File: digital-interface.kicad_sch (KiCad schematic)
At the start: 33 parts, among them U701 Si8641BD-B-IS2, U702 R05C05TE05S

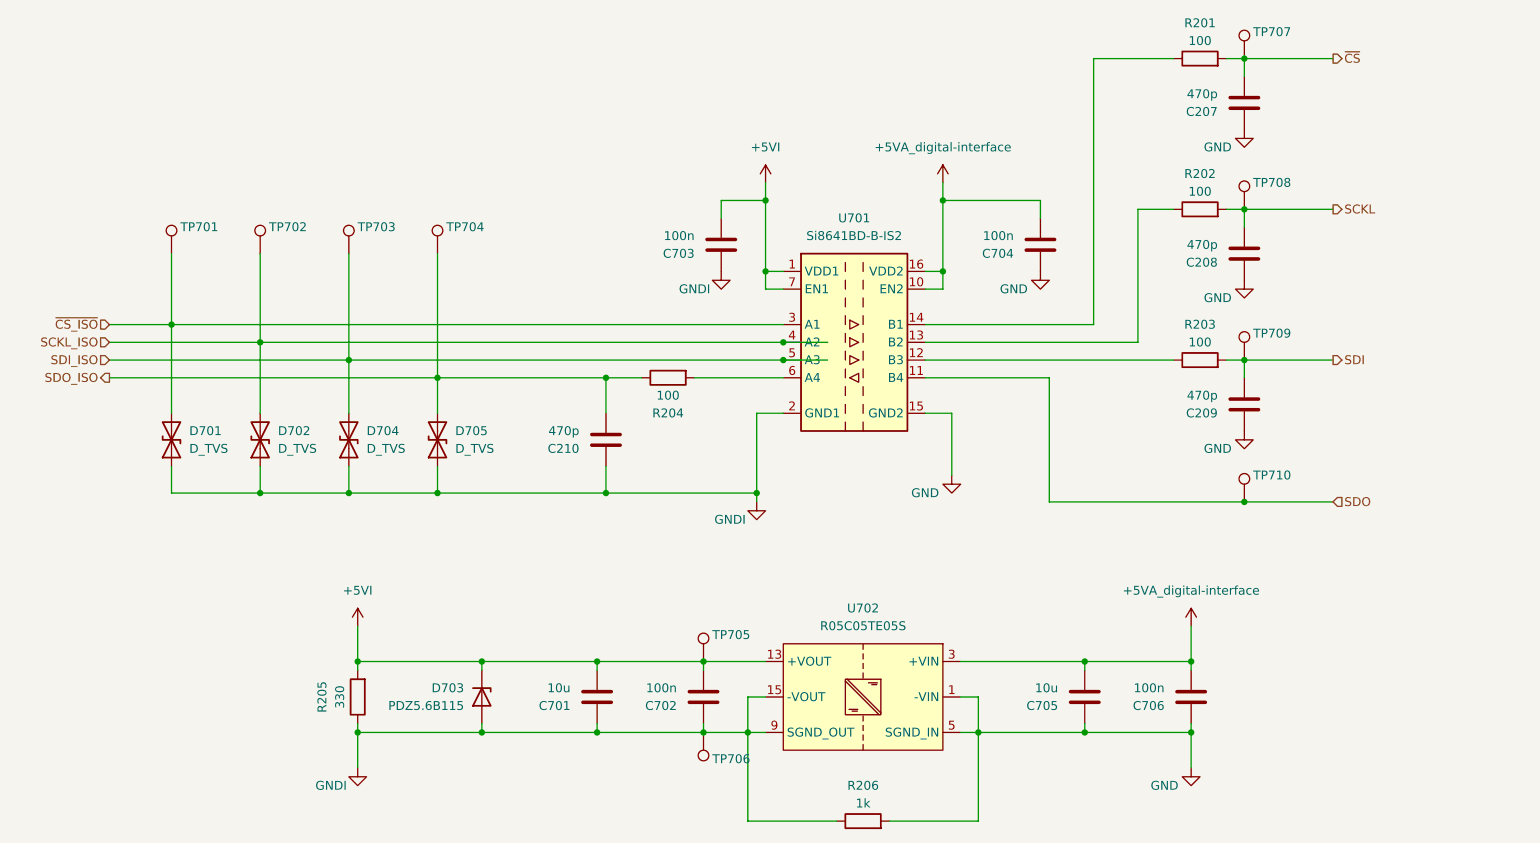
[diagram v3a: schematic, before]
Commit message: reannotate enclosure digital-interface
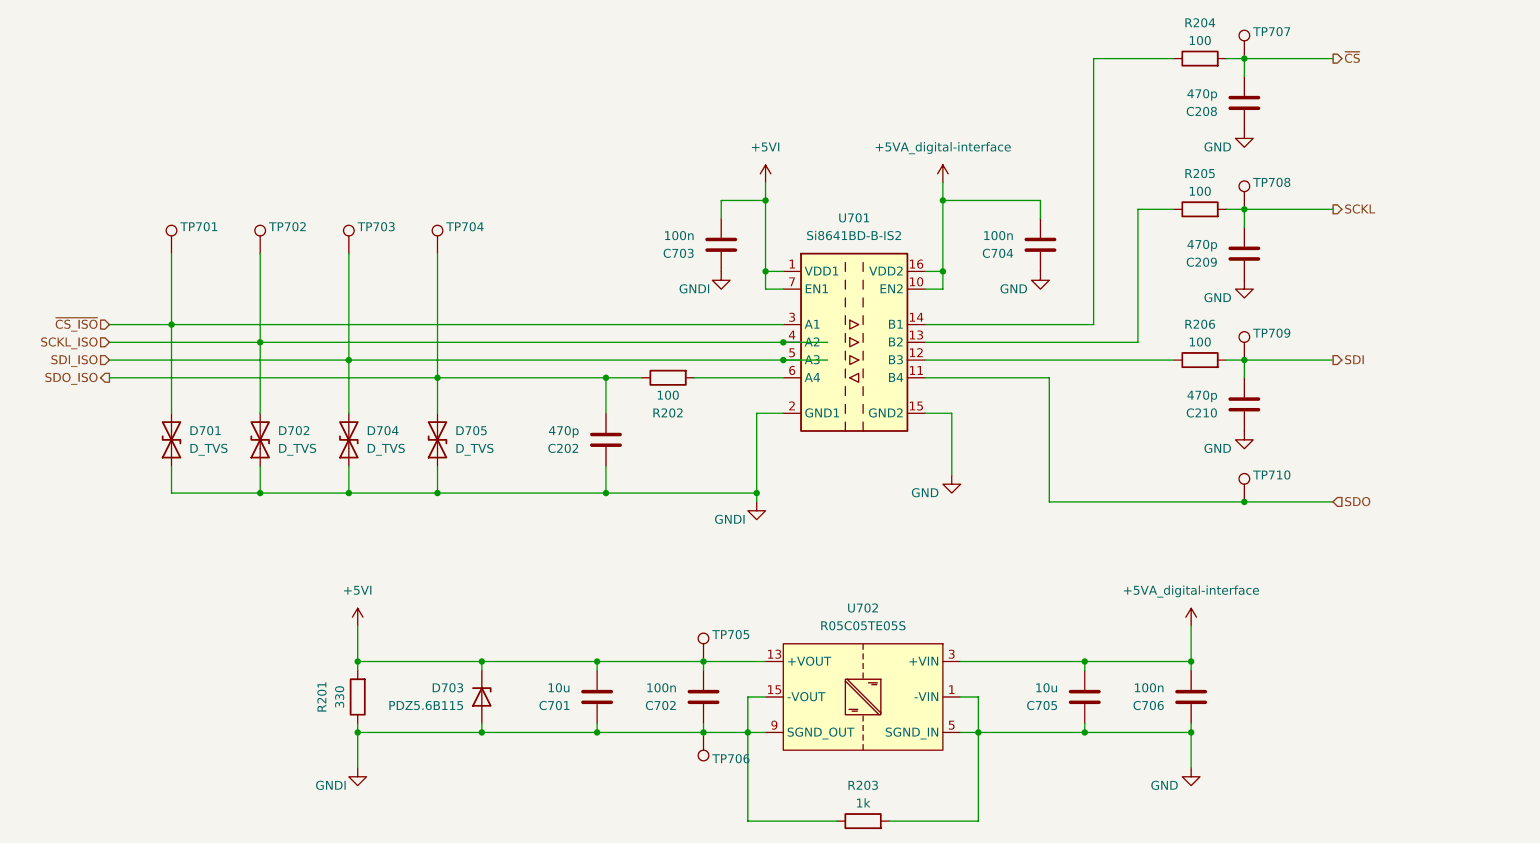
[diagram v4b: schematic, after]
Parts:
- renumbered C210 to C202, C207 to C208, C208 to C209, C209 to C210, R205 to R201, R204 to R202, R206 to R203, R201 to R204, R202 to R205, R203 to R206
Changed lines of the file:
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@@
 		(on_board yes)
 		(dnp no)
-		(property "Reference" "C207"
+		(property "Reference" "C208"
 			(at 199.39 38.1001 0)
 			(effects
@@
 			(project "enclosure"
 				(path "/8ec0899b-9d7b-491d-933a-49b74b34a0df/dc44c087-3b63-4db9-8fc8-89acb3b8154a"
-					(reference "C207")
+					(reference "C208")
 					(unit 1)
 				)
@@
 			(project "enclosure"
 				(path "/8ec0899b-9d7b-491d-933a-49b74b34a0df/dc44c087-3b63-4db9-8fc8-89acb3b8154a"
-					(reference "C206")
+					(reference "C207")
 					(unit 1)
 				)
@@
 			(project "enclosure"
 				(path "/8ec0899b-9d7b-491d-933a-49b74b34a0df/dc44c087-3b63-4db9-8fc8-89acb3b8154a"
-					(reference "#PWR204")
+					(reference "#PWR0204")
 					(unit 1)
 				)
@@
 			(project "enclosure"
 				(path "/8ec0899b-9d7b-491d-933a-49b74b34a0df/dc44c087-3b63-4db9-8fc8-89acb3b8154a"
-					(reference "C204")
+					(reference "C205")
 					(unit 1)
 				)
@@
 			(project "enclosure"
 				(path "/8ec0899b-9d7b-491d-933a-49b74b34a0df/dc44c087-3b63-4db9-8fc8-89acb3b8154a"
-					(reference "#PWR209")
+					(reference "#PWR0209")
 					(unit 1)
 				)
@@
 			(project "enclosure"
 				(path "/8ec0899b-9d7b-491d-933a-49b74b34a0df/dc44c087-3b63-4db9-8fc8-89acb3b8154a"
-					(reference "#PWR206")
+					(reference "#PWR0206")
 					(unit 1)
 				)
@@
 		(on_board yes)
 		(dnp no)
-		(property "Reference" "R204"
+		(property "Reference" "R202"
 			(at 120.65 81.28 90)
 			(effects
@@
 			(project "enclosure"
 				(path "/8ec0899b-9d7b-491d-933a-49b74b34a0df/dc44c087-3b63-4db9-8fc8-89acb3b8154a"
-					(reference "R204")
+					(reference "R202")
 					(unit 1)
 				)
@@
 			(project "enclosure"
 				(path "/8ec0899b-9d7b-491d-933a-49b74b34a0df/dc44c087-3b63-4db9-8fc8-89acb3b8154a"
-					(reference "C205")
+					(reference "C206")
 					(unit 1)
 				)
@@
 		(on_board yes)
 		(dnp no)
-		(property "Reference" "R206"
+		(property "Reference" "R203"
 			(at 148.59 134.62 90)
 			(effects
@@
 			(project "enclosure"
 				(path "/8ec0899b-9d7b-491d-933a-49b74b34a0df/dc44c087-3b63-4db9-8fc8-89acb3b8154a"
-					(reference "R206")
+					(reference "R203")
 					(unit 1)
 				)
@@
 			(project "enclosure"
 				(path "/8ec0899b-9d7b-491d-933a-49b74b34a0df/dc44c087-3b63-4db9-8fc8-89acb3b8154a"
-					(reference "#PWR210")
+					(reference "#PWR0210")
 					(unit 1)
 				)
@@
 		(on_board yes)
 		(dnp no)
-		(property "Reference" "R201"
+		(property "Reference" "R204"
 			(at 196.85 25.4 90)
 			(effects
@@
 			(project "enclosure"
 				(path "/8ec0899b-9d7b-491d-933a-49b74b34a0df/dc44c087-3b63-4db9-8fc8-89acb3b8154a"
-					(reference "R201")
+					(reference "R204")
 					(unit 1)
 				)
@@
 			(project "enclosure"
 				(path "/8ec0899b-9d7b-491d-933a-49b74b34a0df/dc44c087-3b63-4db9-8fc8-89acb3b8154a"
-					(reference "D203")
+					(reference "D205")
 					(unit 1)
 				)
@@
 		(on_board yes)
 		(dnp no)
-		(property "Reference" "C209"
+		(property "Reference" "C210"
 			(at 199.39 81.2801 0)
 			(effects
@@
 			(project "enclosure"
 				(path "/8ec0899b-9d7b-491d-933a-49b74b34a0df/dc44c087-3b63-4db9-8fc8-89acb3b8154a"
-					(reference "C209")
+					(reference "C210")
 					(unit 1)
 				)
@@
 			(project "enclosure"
 				(path "/8ec0899b-9d7b-491d-933a-49b74b34a0df/dc44c087-3b63-4db9-8fc8-89acb3b8154a"
-					(reference "#PWR201")
+					(reference "#PWR0201")
 					(unit 1)
 				)
@@
 		(on_board yes)
 		(dnp no)
-		(property "Reference" "R205"
+		(property "Reference" "R201"
 			(at 71.12 121.92 90)
 			(effects
@@
 			(project "enclosure"
 				(path "/8ec0899b-9d7b-491d-933a-49b74b34a0df/dc44c087-3b63-4db9-8fc8-89acb3b8154a"
-					(reference "R205")
+					(reference "R201")
 					(unit 1)
 				)
@@
 			(project "enclosure"
 				(path "/8ec0899b-9d7b-491d-933a-49b74b34a0df/dc44c087-3b63-4db9-8fc8-89acb3b8154a"
-					(reference "#PWR205")
+					(reference "#PWR0205")
 					(unit 1)
 				)
@@
 			(project "enclosure"
 				(path "/8ec0899b-9d7b-491d-933a-49b74b34a0df/dc44c087-3b63-4db9-8fc8-89acb3b8154a"
-					(reference "#PWR202")
+					(reference "#PWR0202")
 					(unit 1)
 				)
@@
 		(on_board yes)
 		(dnp no)
-		(property "Reference" "C208"
+		(property "Reference" "C209"
 			(at 199.39 59.6901 0)
 			(effects
@@
 			(project "enclosure"
 				(path "/8ec0899b-9d7b-491d-933a-49b74b34a0df/dc44c087-3b63-4db9-8fc8-89acb3b8154a"
-					(reference "C208")
+					(reference "C209")
 					(unit 1)
 				)
@@
 		(on_board yes)
 		(dnp no)
-		(property "Reference" "#PWR0213"
+		(property "Reference" "#PWR0211"
 			(at 203.2 46.99 0)
 			(effects
@@
 			(project "enclosure"
 				(path "/8ec0899b-9d7b-491d-933a-49b74b34a0df/dc44c087-3b63-4db9-8fc8-89acb3b8154a"
-					(reference "#PWR0213")
+					(reference "#PWR0211")
 					(unit 1)
 				)
@@
 			(project "enclosure"
 				(path "/8ec0899b-9d7b-491d-933a-49b74b34a0df/dc44c087-3b63-4db9-8fc8-89acb3b8154a"
-					(reference "D204")
+					(reference "D203")
 					(unit 1)
 				)
@@
 		(on_board yes)
 		(dnp no)
-		(property "Reference" "R202"
+		(property "Reference" "R205"
 			(at 196.85 46.99 90)
 			(effects
@@
 			(project "enclosure"
 				(path "/8ec0899b-9d7b-491d-933a-49b74b34a0df/dc44c087-3b63-4db9-8fc8-89acb3b8154a"
-					(reference "R202")
+					(reference "R205")
 					(unit 1)
 				)
@@
 		(on_board yes)
 		(dnp no)
-		(property "Reference" "#PWR0211"
+		(property "Reference" "#PWR0213"
 			(at 203.2 90.17 0)
 			(effects
@@
 			(project "enclosure"
 				(path "/8ec0899b-9d7b-491d-933a-49b74b34a0df/dc44c087-3b63-4db9-8fc8-89acb3b8154a"
-					(reference "#PWR0211")
+					(reference "#PWR0213")
 					(unit 1)
 				)
@@
 		(on_board yes)
 		(dnp no)
-		(property "Reference" "R203"
+		(property "Reference" "R206"
 			(at 196.85 68.58 90)
 			(effects
@@
 			(project "enclosure"
 				(path "/8ec0899b-9d7b-491d-933a-49b74b34a0df/dc44c087-3b63-4db9-8fc8-89acb3b8154a"
-					(reference "R203")
+					(reference "R206")
 					(unit 1)
 				)
@@
 			(project "enclosure"
 				(path "/8ec0899b-9d7b-491d-933a-49b74b34a0df/dc44c087-3b63-4db9-8fc8-89acb3b8154a"
-					(reference "#PWR207")
+					(reference "#PWR0207")
 					(unit 1)
 				)
@@
 			(project "enclosure"
 				(path "/8ec0899b-9d7b-491d-933a-49b74b34a0df/dc44c087-3b63-4db9-8fc8-89acb3b8154a"
-					(reference "#PWR208")
+					(reference "#PWR0208")
 					(unit 1)
 				)
@@
 			(project "enclosure"
 				(path "/8ec0899b-9d7b-491d-933a-49b74b34a0df/dc44c087-3b63-4db9-8fc8-89acb3b8154a"
-					(reference "C202")
+					(reference "C203")
 					(unit 1)
 				)
@@
 			(project "enclosure"
 				(path "/8ec0899b-9d7b-491d-933a-49b74b34a0df/dc44c087-3b63-4db9-8fc8-89acb3b8154a"
-					(reference "#PWR203")
+					(reference "#PWR0203")
 					(unit 1)
 				)
@@
 			(project "enclosure"
 				(path "/8ec0899b-9d7b-491d-933a-49b74b34a0df/dc44c087-3b63-4db9-8fc8-89acb3b8154a"
-					(reference "D205")
+					(reference "D204")
 					(unit 1)
 				)
@@
 		(on_board yes)
 		(dnp no)
-		(property "Reference" "C210"
+		(property "Reference" "C202"
 			(at 107.95 86.3601 0)
 			(effects
@@
 			(project "enclosure"
 				(path "/8ec0899b-9d7b-491d-933a-49b74b34a0df/dc44c087-3b63-4db9-8fc8-89acb3b8154a"
-					(reference "C210")
+					(reference "C202")
 					(unit 1)
 				)
@@
 			(project "enclosure"
 				(path "/8ec0899b-9d7b-491d-933a-49b74b34a0df/dc44c087-3b63-4db9-8fc8-89acb3b8154a"
-					(reference "C203")
+					(reference "C204")
 					(unit 1)
 				)

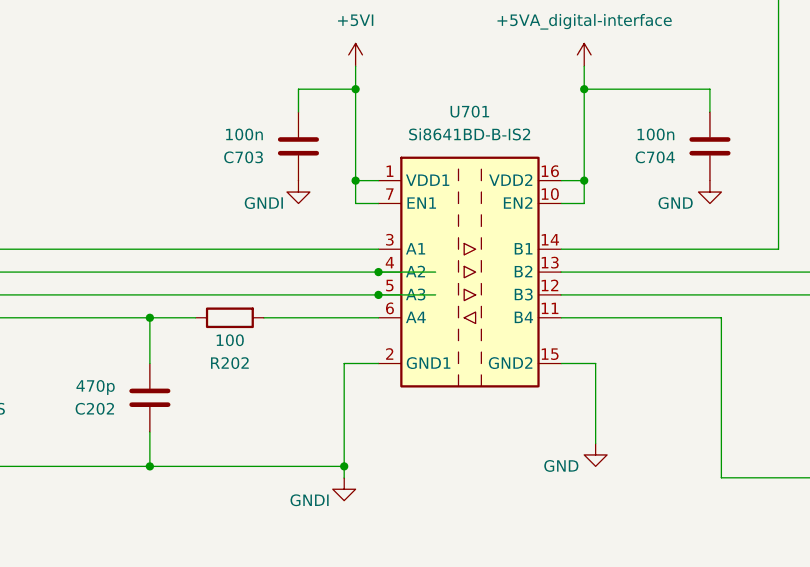
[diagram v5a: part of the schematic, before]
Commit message: fix enclosure digital-interface stray wire in schmematic
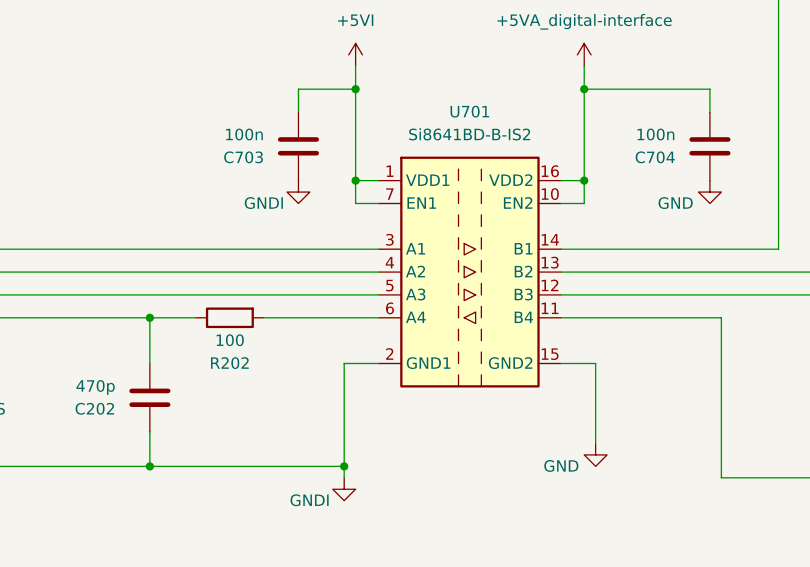
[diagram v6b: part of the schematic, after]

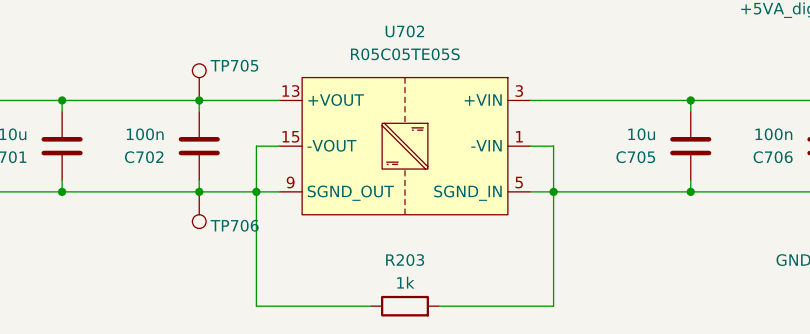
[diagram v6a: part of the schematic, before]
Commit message: fix enclosure digital-interface esd protection resistor shall be 1MR not 1kR
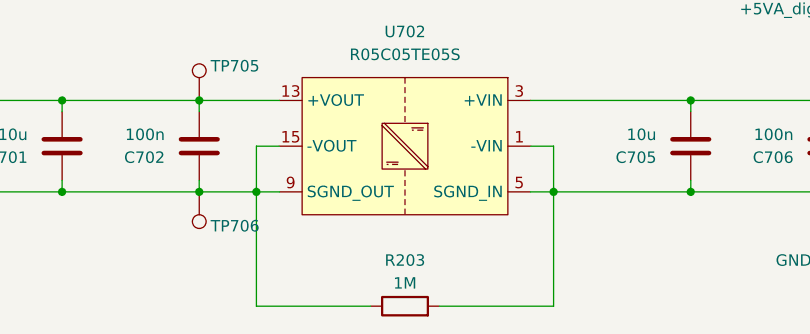
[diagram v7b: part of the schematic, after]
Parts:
- R203: value 1k -> 1M; MPN RC1210FR-071KL -> RC1210FR-071ML; VPN 603-RC1210FR-071KL -> 603-RC1210FR-071ML
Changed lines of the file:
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@@
 			)
 		)
-		(property "Value" "1k"
+		(property "Value" "1M"
 			(at 148.59 137.16 90)
 			(effects
@@
 			)
 		)
-		(property "MPN" "RC1210FR-071KL"
+		(property "MPN" "RC1210FR-071ML"
 			(at 148.59 139.7 0)
 			(effects
@@
 			)
 		)
-		(property "VPN" "603-RC1210FR-071KL"
+		(property "VPN" "603-RC1210FR-071ML"
 			(at 148.59 139.7 0)
 			(effects

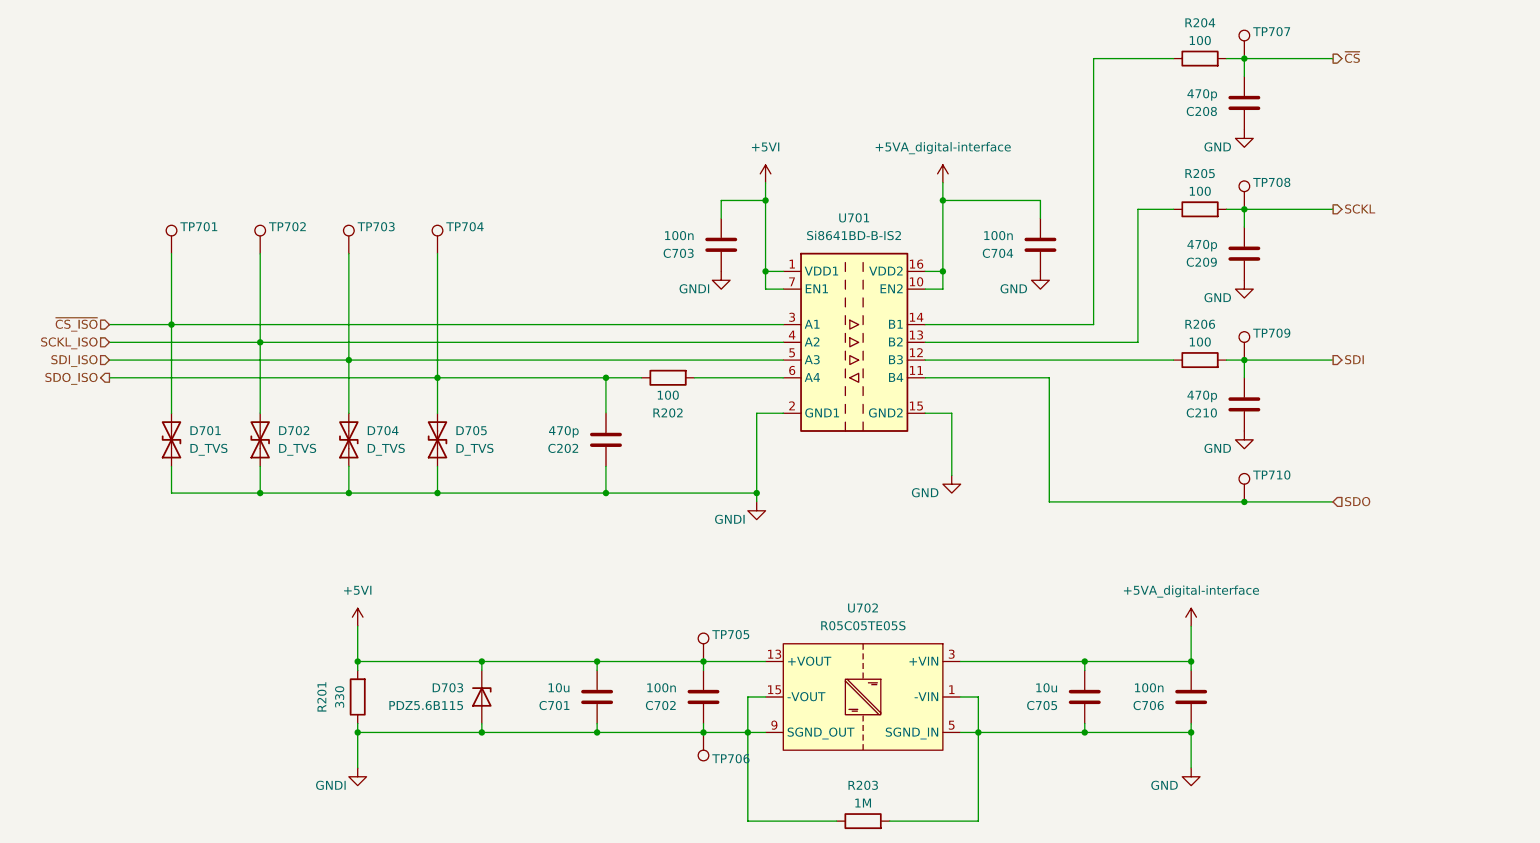
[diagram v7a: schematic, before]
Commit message: add enclosure digital-interface pull down resistors at inputs
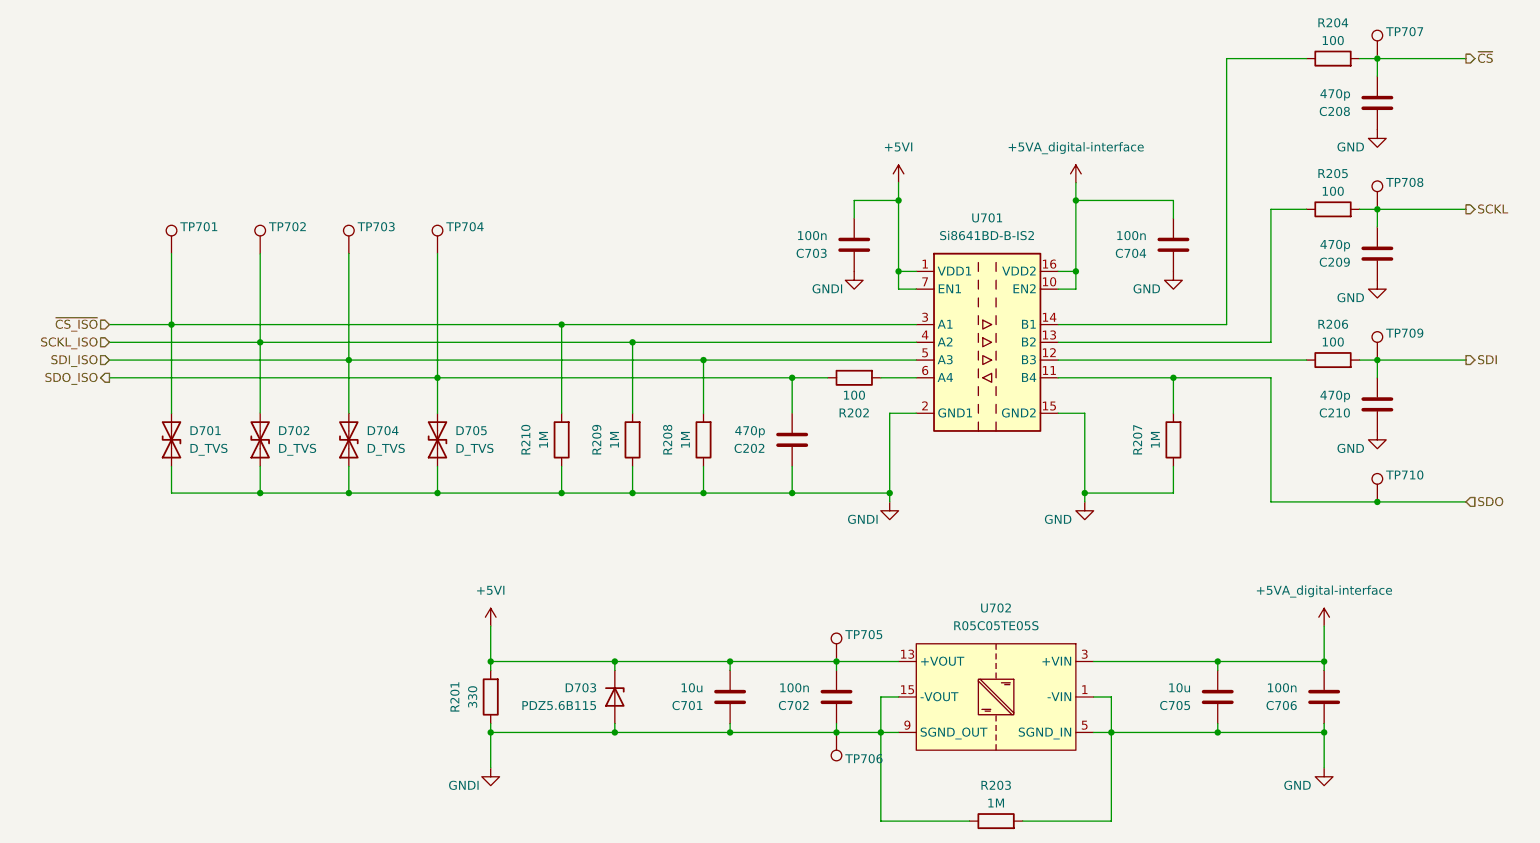
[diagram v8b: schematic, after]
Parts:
- added R207, R208, R209, R210: 1M, pss:R_1210_3225Metric_Pad1.30x2.65mm_HandSolder, symbol enclosure:R
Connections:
- net GND: now also R207.1
- net GNDI: now also R208.1, R209.1, R210.1
- net SCKL_ISO: now also R209.2
- net SDI_ISO: now also R208.2
- net SDO: now also R207.2
- net ~{CS_ISO}: now also R210.2
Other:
- moved on the sheet: C202, C208, C209, C210, C701, C702, C703, C704, C705, C706, D703, R201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
